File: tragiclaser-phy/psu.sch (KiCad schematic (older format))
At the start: 7 parts, among them K1 CONN_3_PWROUT, U2 ADP322ACPZ-145-R7

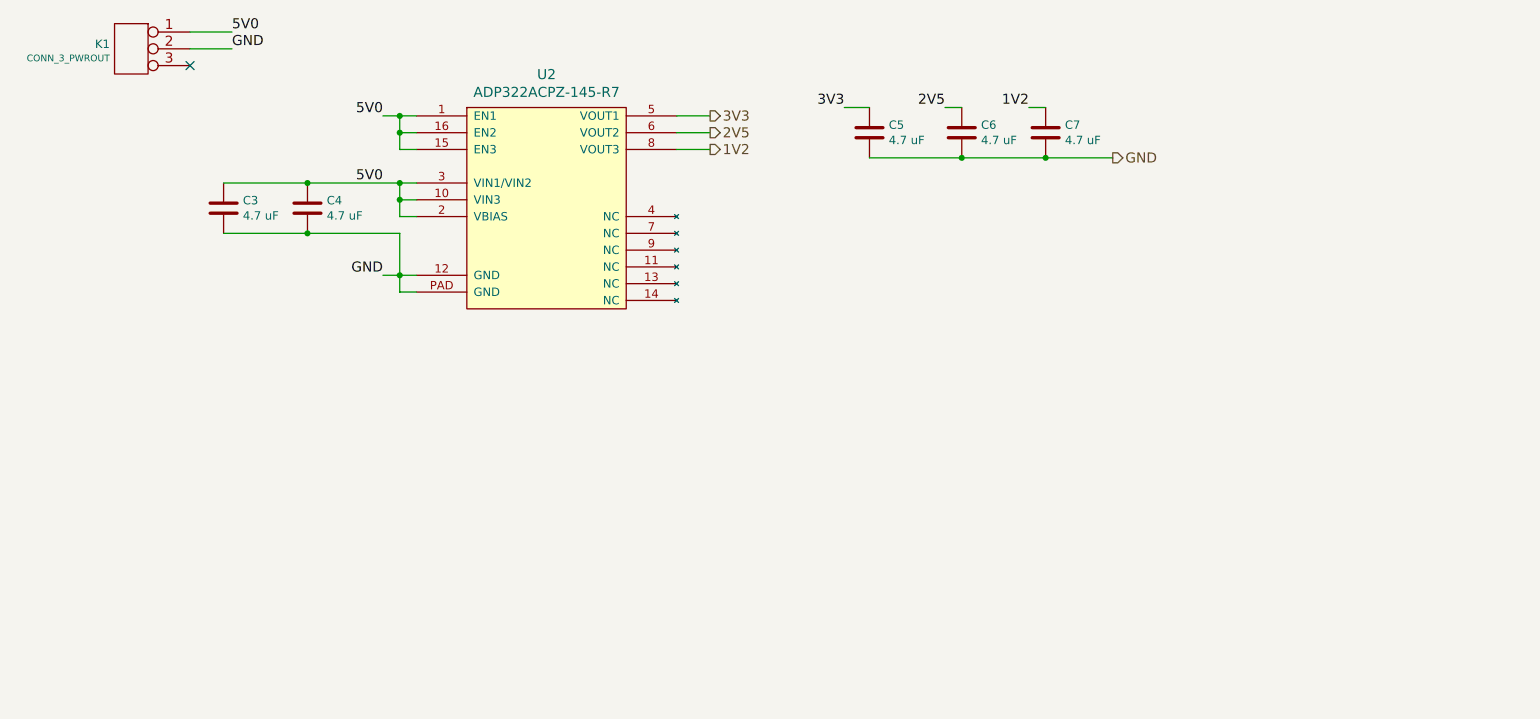
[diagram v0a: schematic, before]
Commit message: Began layout on TRAGICLASER PHY
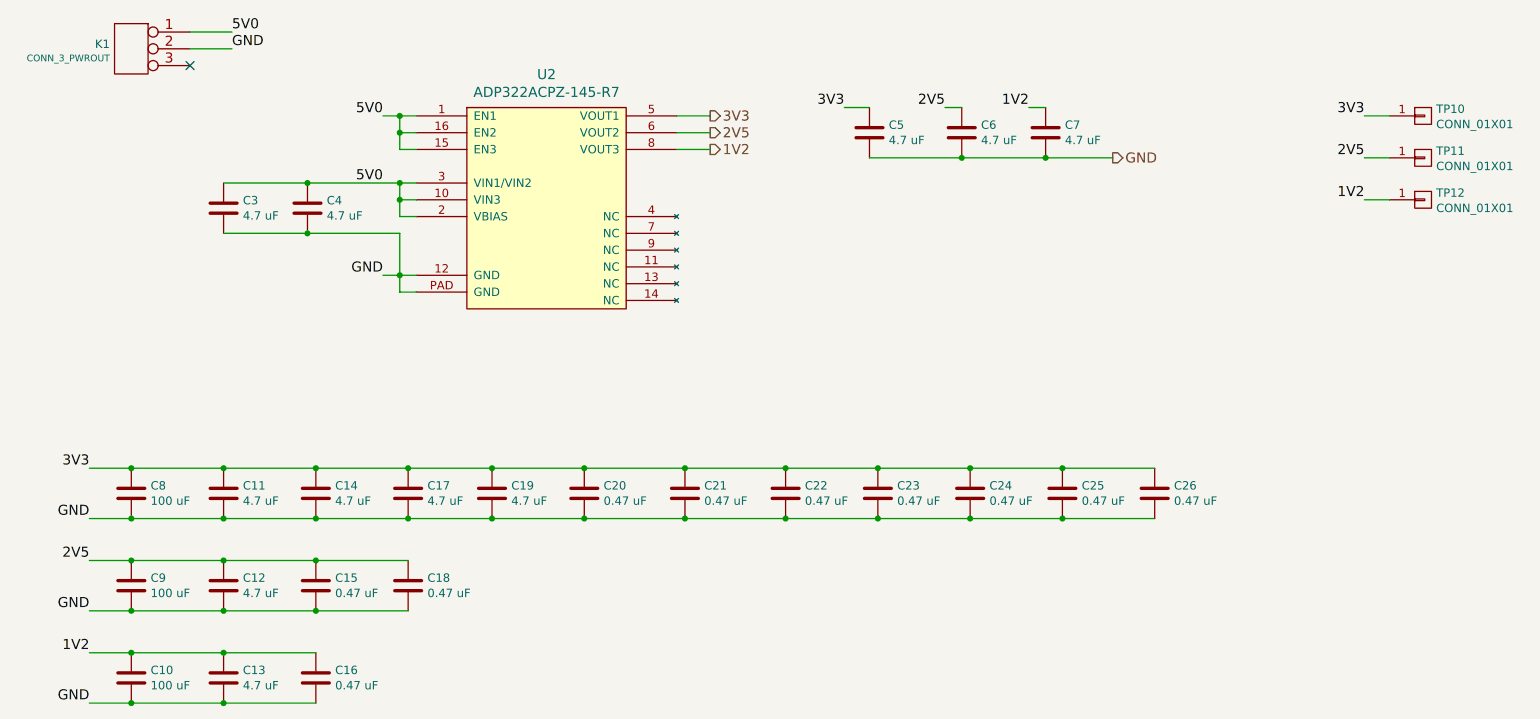
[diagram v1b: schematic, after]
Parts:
- added C10, C8, C9: 100 uF, azonenberg_pcb:EIA_1206_CAP_NOSILK, symbol C
- added C11, C12, C13, C14, C17, C19: 4.7 uF, azonenberg_pcb:EIA_0603_CAP_NOSILK, symbol C
- added C15, C16, C18, C20, C21, C22, C23, C24, C25, C26: 0.47 uF, azonenberg_pcb:EIA_0402_CAP_NOSILK, symbol C
- added TP10, TP11, TP12: CONN_01X01, azonenberg_pcb:TESTPOINT_SMT_0.5MM, symbol CONN_01X01
- C3, C4, C5, C6, C7: footprint (none) -> azonenberg_pcb:EIA_0603_CAP_NOSILK
- K1: footprint (none) -> azonenberg_pcb:CONN_CUI_PJ-058BH_HIPWR_BARREL_NOSLOT
- U2: footprint (none) -> azonenberg_pcb:QFN_16_0.5MM_3x3MM
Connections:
- net 1V2: now also C10.1, C13.1, C16.1, TP12.1 (P1)
- net 2V5: now also C12.1, C15.1, C18.1, C9.1, TP11.1 (P1)
- net 3V3: now also C11.1, C14.1, C17.1, C19.1, C20.1, C21.1, C22.1, C23.1, C24.1, C25.1, C26.1, C8.1, TP10.1 (P1)
- net GND: now also C10.2, C11.2, C12.2, C13.2, C14.2, C15.2, C16.2, C17.2, C18.2, C19.2, C20.2, C21.2, C22.2, C23.2, C24.2, C25.2, C26.2, C8.2, C9.2
